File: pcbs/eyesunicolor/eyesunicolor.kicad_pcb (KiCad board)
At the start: 2 copper layers, 21 parts, among them J1 SUPP28, P1 CONN_5X2

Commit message: Dise?o de placa. Acomodamos los leds.
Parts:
- moved D6 387.9 mm to (377.4, 89.4)
- moved D7 378.0 mm to (370.8, 73.2)
- moved D4 369.6 mm to (358.6, 89.4)
- moved D8 368.7 mm to (364.2, 56.9)
- moved D5 368.4 mm to (360.2, 77.2)
- moved D9 360.9 mm to (358.6, 40.1)
- moved D10 357.4 mm to (352.6, 58.4)
- moved D3 351.4 mm to (339.9, 89.4)
- moved D16 350.5 mm to (341.9, 77.2)
- moved D14 346.9 mm to (343.4, 49.3)
- moved D15 343.0 mm to (336.8, 65.0)
- moved D13 333.3 mm to (328.2, 58.4)
- moved D2 333.3 mm to (321.1, 89.4)
- moved D12 327.2 mm to (318.0, 77.2)
- moved D11 320.1 mm to (312.9, 67.6)
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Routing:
- net /BLANK: track 18.0 -> 0.00 mm
- net VCC: track 18.0 -> 0.00 mm

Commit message: Termine la placa. Hay que optimizarla.
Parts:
- R1: value R -> 2.2k
- R2: value R -> 10k
- moved R2 22.9 mm to (321.1, 142.2), turned to 90 degrees
- moved C1 13.3 mm to (335.8, 145.8), turned to 0 degrees
- moved R1 13.2 mm to (316.0, 140.2), turned to 270 degrees
- turned P1 to 180 degrees
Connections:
- D1 pad 2: N-0000020 -> N-0000013
- D10 pad 2: N-0000019 -> N-0000026
- D11 pad 2: N-0000018 -> N-0000029
- D12 pad 2: N-0000017 -> N-0000018
- D13 pad 2: N-0000016 -> N-0000020
- D14 pad 2: N-0000015 -> N-0000017
- D15 pad 2: N-0000014 -> N-0000028
- D16 pad 2: N-0000029 -> N-0000027
- D2 pad 2: N-0000021 -> N-0000019
- D3 pad 2: N-0000022 -> N-0000012
- D6 pad 2: N-0000025 (its old number) -> N-0000016
- D7 pad 2: N-0000026 -> N-0000022
- D8 pad 2: N-0000027 -> N-0000023
- D9 pad 2: N-0000028 -> N-0000021
- J1 pad 1: N-0000020 -> N-0000022
- J1 pad 10: N-0000019 -> N-0000028
- J1 pad 11: N-0000018 -> N-0000020
- J1 pad 12: N-0000017 -> N-0000019
- J1 pad 13: N-0000016 -> N-0000018
- J1 pad 14: N-0000015 -> N-0000029
- J1 pad 15: N-0000029 -> N-0000013
- J1 pad 2: N-0000021 -> N-0000023
- J1 pad 28: N-0000014 -> N-0000016
- J1 pad 3: N-0000022 -> N-0000024
- J1 pad 5: N-0000024 -> N-0000021
- J1 pad 6: N-0000025 (its old number) -> N-0000026
- J1 pad 7: N-0000026 -> N-0000017
- J1 pad 8: N-0000027 -> N-0000012
- J1 pad 9: N-0000028 -> N-0000027
- P1 pad 10: (no net) -> GND
- P1 pad 2: /IREF -> /GSCLK
- P1 pad 4: /GSCLK -> (no net)
- P1 pad 6: VCC -> /IREF
- P1 pad 8: GND -> VCC
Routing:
- net /GSCLK: track 0.00 -> 105.0 mm
- net /IREF: track 0.00 -> 90.5 mm
- net N-0000021: track 0.00 -> 81.5 mm
- net VCC: track 0.00 -> 73.1 mm
- net N-0000017: track 0.00 -> 70.0 mm
- net N-0000023: track 0.00 -> 66.6 mm
- net GND: track 0.00 -> 62.3 mm
- net N-0000026: track 0.00 -> 61.7 mm
- net N-0000020: track 0.00 -> 56.9 mm
- net N-0000028: track 0.00 -> 53.3 mm
- net N-0000029: track 0.00 -> 52.8 mm
- net N-0000022: track 0.00 -> 49.3 mm
- net N-0000016: track 0.00 -> 46.4 mm
- net N-0000024: track 0.00 -> 45.7 mm
- net N-0000018: track 0.00 -> 41.7 mm
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
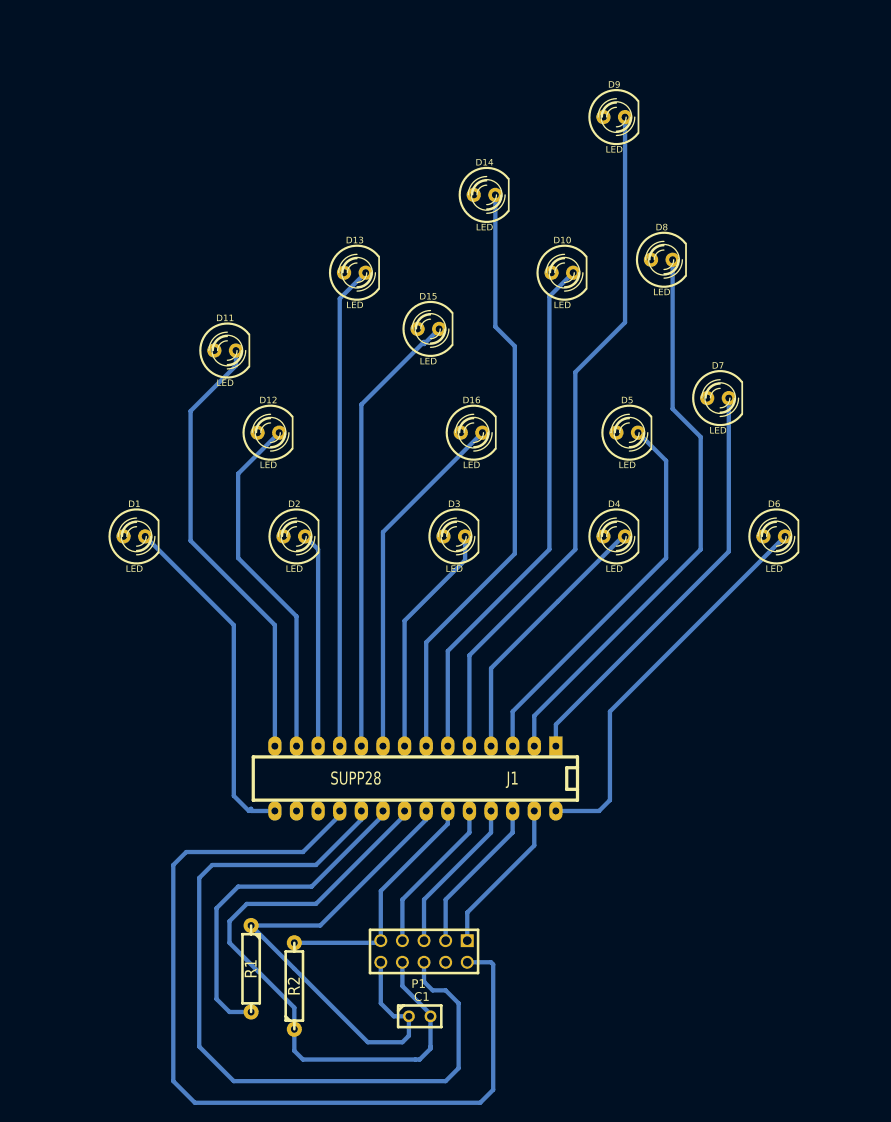
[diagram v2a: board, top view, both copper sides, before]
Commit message: Se termino el PCB del ojo izquierdo, se comenzo a trabajar con el ojo derecho
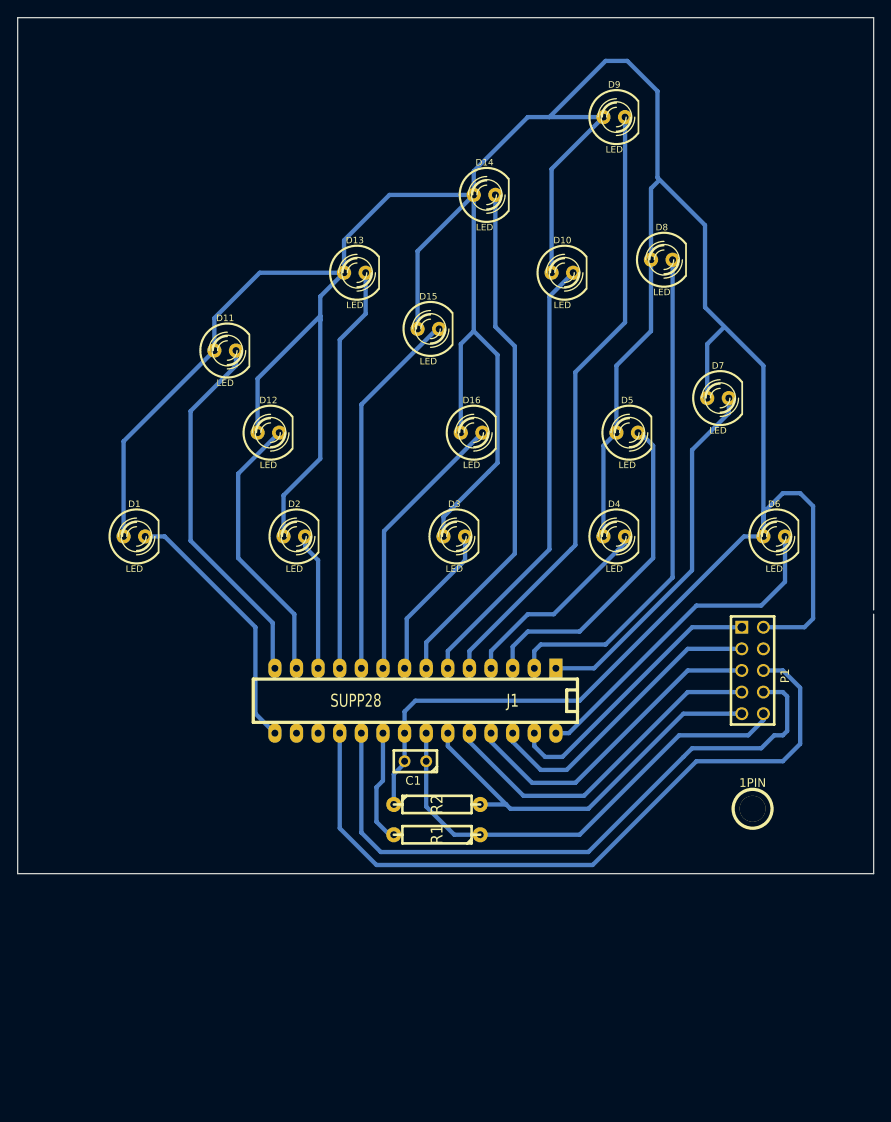
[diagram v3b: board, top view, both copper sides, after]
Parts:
- added 1PIN: P***, 1pin, F.Cu at (374.9, 121.4)
- moved P1 50.8 mm to (374.9, 105.2), turned to 270 degrees
- moved C1 30.0 mm to (335.3, 115.8), turned to 180 degrees
- moved R2 27.1 mm to (337.8, 120.9), turned to 0 degrees
- moved R1 26.9 mm to (337.8, 124.5), turned to 180 degrees
- moved J1 9.14 mm to (335.3, 108.7)
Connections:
- P1 pad 2: /GSCLK -> VCC
- P1 pad 6: /IREF -> /GSCLK
- P1 pad 8: VCC -> /IREF
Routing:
- net VCC: track 73.1 -> 455.8 mm
- net N-0000010: track 40.0 -> 13.4 mm
- net /XLAT: track 18.5 -> 40.7 mm
- net /GSCLK: track 105.0 -> 84.7 mm
- net /SCLK: track 18.5 -> 37.9 mm
- net /BLANK: track 28.8 -> 46.8 mm
- net /SIN: track 18.5 -> 35.9 mm
- net /IREF: track 90.5 -> 75.6 mm
- net /VPRG: track 18.5 -> 32.7 mm
- net N-0000013: track 40.7 -> 30.8 mm
- net N-0000028: track 53.3 -> 43.8 mm
- net N-0000029: track 52.8 -> 43.7 mm
- net N-0000012: track 27.6 -> 18.4 mm
- net N-0000026: track 61.7 -> 52.6 mm
- net N-0000021: track 81.5 -> 72.3 mm
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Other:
- board outline added: 100.6 x 100.6 mm

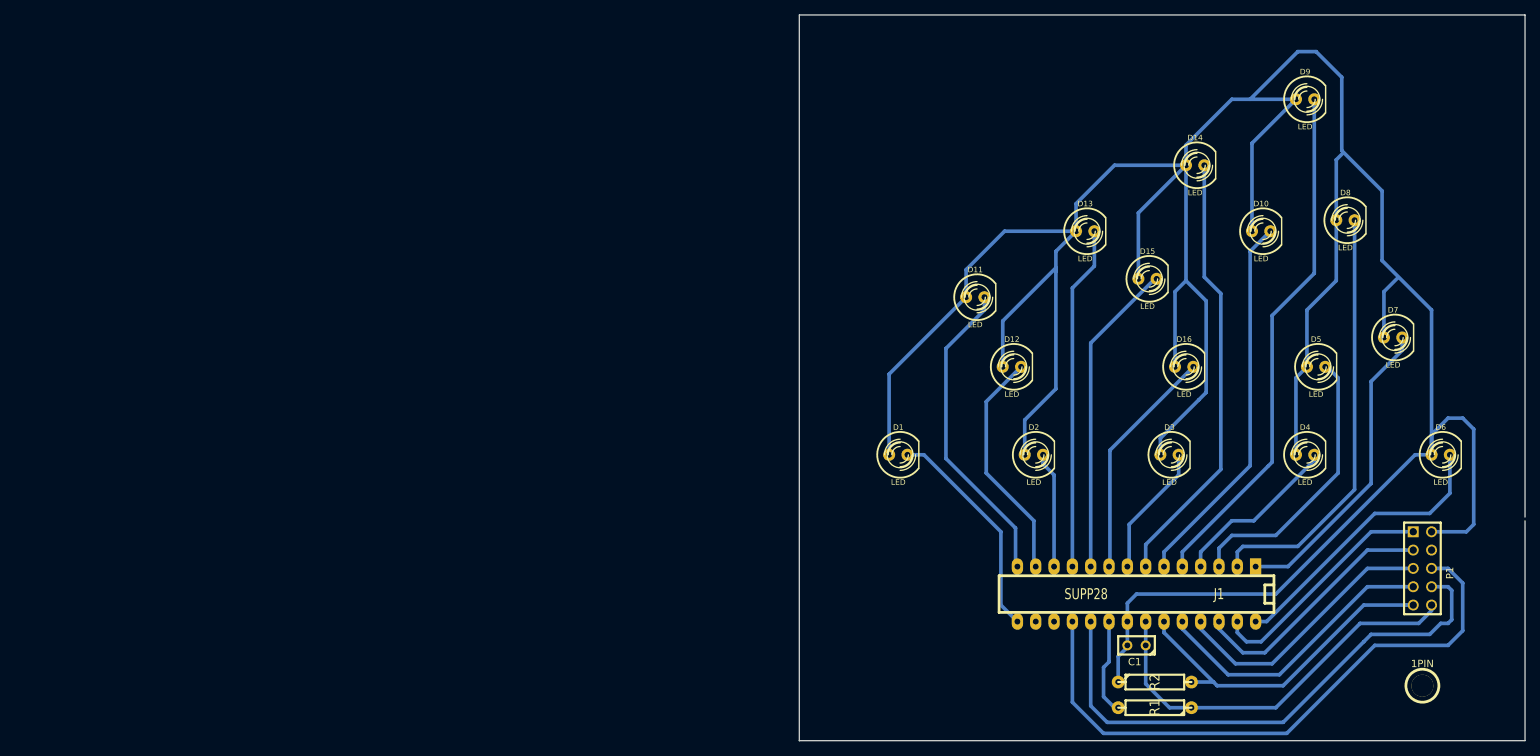
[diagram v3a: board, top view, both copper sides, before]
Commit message: Arme el pcb del ojo derecho. Falta termiar
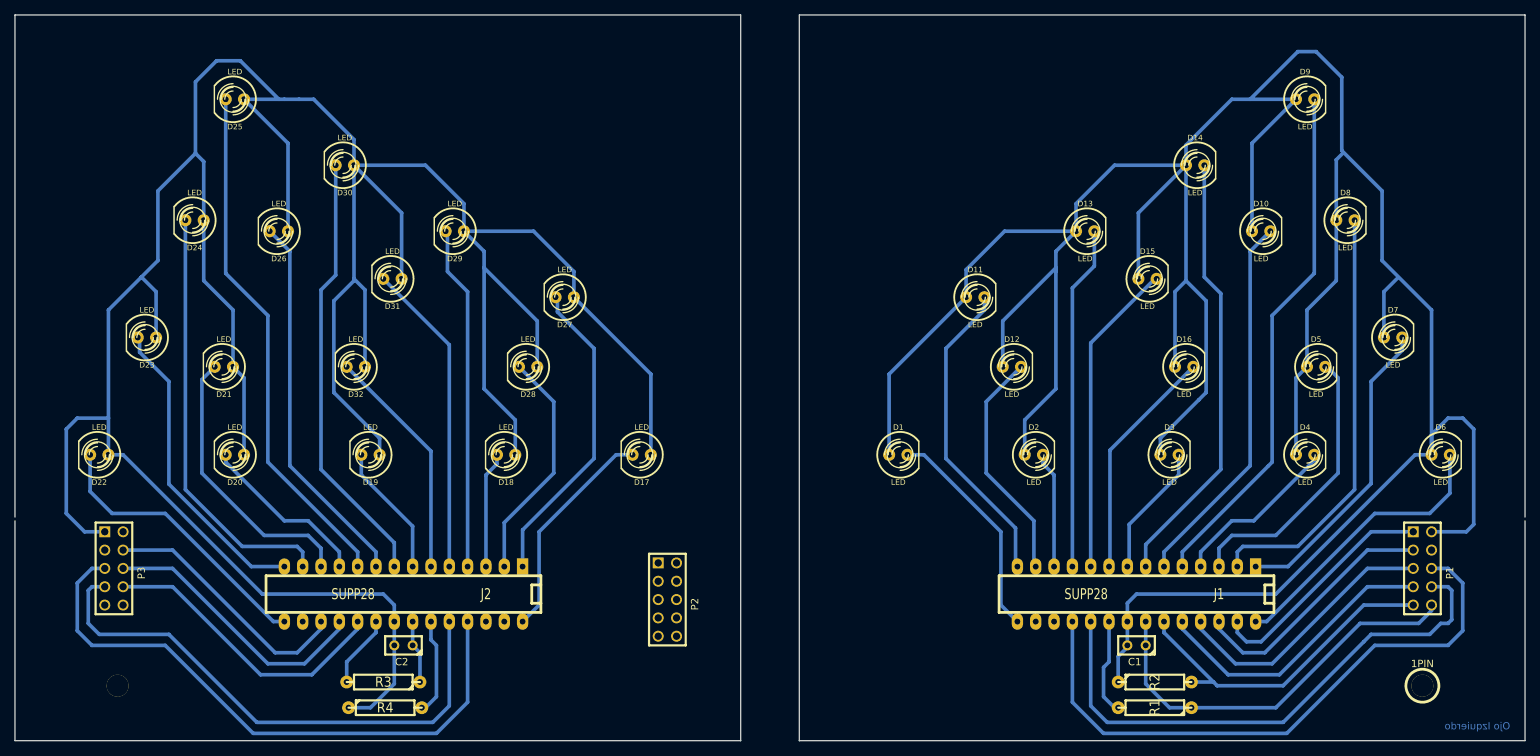
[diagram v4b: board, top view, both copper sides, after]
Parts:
- added 1PIN: P***, 1pin, B.Cu at (194.1, 121.4)
- added C2: C, C1, F.Cu at (233.7, 115.8)
- added D17: LED, LED-5MM, F.Cu at (266.7, 89.4)
- added D18: LED, LED-5MM, F.Cu at (247.9, 89.4)
- added D19: LED, LED-5MM, F.Cu at (229.1, 89.4)
- added D20: LED, LED-5MM, F.Cu at (210.3, 89.4)
- added D21: LED, LED-5MM, F.Cu at (208.8, 77.2)
- added D22: LED, LED-5MM, F.Cu at (191.5, 89.4)
- added D23: LED, LED-5MM, F.Cu at (198.1, 73.2)
- added D24: LED, LED-5MM, F.Cu at (204.7, 56.9)
- added D25: LED, LED-5MM, F.Cu at (210.3, 40.1)
- added D26: LED, LED-5MM, F.Cu at (216.4, 58.4)
- added D27: LED, LED-5MM, F.Cu at (256.0, 67.6)
- added D28: LED, LED-5MM, F.Cu at (251.0, 77.2)
- added D29: LED, LED-5MM, F.Cu at (240.8, 58.4)
- added D30: LED, LED-5MM, F.Cu at (225.6, 49.3)
- added D31: LED, LED-5MM, F.Cu at (232.2, 65.0)
- added D32: LED, LED-5MM, F.Cu at (227.1, 77.2)
- added J2: SUPP28, DIP-28__300_ELL, F.Cu at (233.7, 108.7)
- added P2: CONN_5X2, PIN_ARRAY_5x2, F.Cu at (270.3, 109.5)
- added P3: CONN_5X2, PIN_ARRAY_5x2, F.Cu at (193.5, 105.2)
- added R3: 2.2k, R4-LARGE_PADS, F.Cu at (230.9, 120.9)
- added R4: 10k, R4-LARGE_PADS, F.Cu at (231.1, 124.5)
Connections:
- net /BLANK renamed /BLANK_I
- net /GSCLK renamed /GSCLK_I
- net /IREF renamed /DCPRG_I
- net /SCLK renamed /SCLK_I
- net /SIN renamed /SIN_I
- net /VPRG renamed /VPRG_I
- net /XLAT renamed /XLAT_I
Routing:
- net VCC: track 455.8 -> 909.2 mm
- net /SCLK_D: track 0.00 -> 84.2 mm
- net /XLAT_D: track 0.00 -> 75.4 mm
- net N-0000054: track 0.00 -> 72.3 mm
- net N-0000014: track 0.00 -> 60.7 mm
- net N-0000057: track 0.00 -> 59.2 mm
- net N-0000042: track 0.00 -> 52.6 mm
- net N-0000043: track 0.00 -> 47.7 mm
- net N-0000049: track 0.00 -> 43.7 mm
- net N-0000046: track 0.00 -> 43.7 mm
- net N-0000041: track 0.00 -> 42.8 mm
- net /DCPRG_D: track 0.00 -> 41.2 mm
- net N-0000055: track 0.00 -> 39.5 mm
- net N-0000051: track 0.00 -> 38.8 mm
- net /GSCLK_D: track 0.00 -> 38.5 mm
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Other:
- board size 100.6 x 100.6 mm -> 209.3 x 100.6 mm
- board text added: "Ojo Izquierdo"

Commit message: Intente terminar los ojos, pero no puedo co el ojo derecho. TERMINAR URGENTE
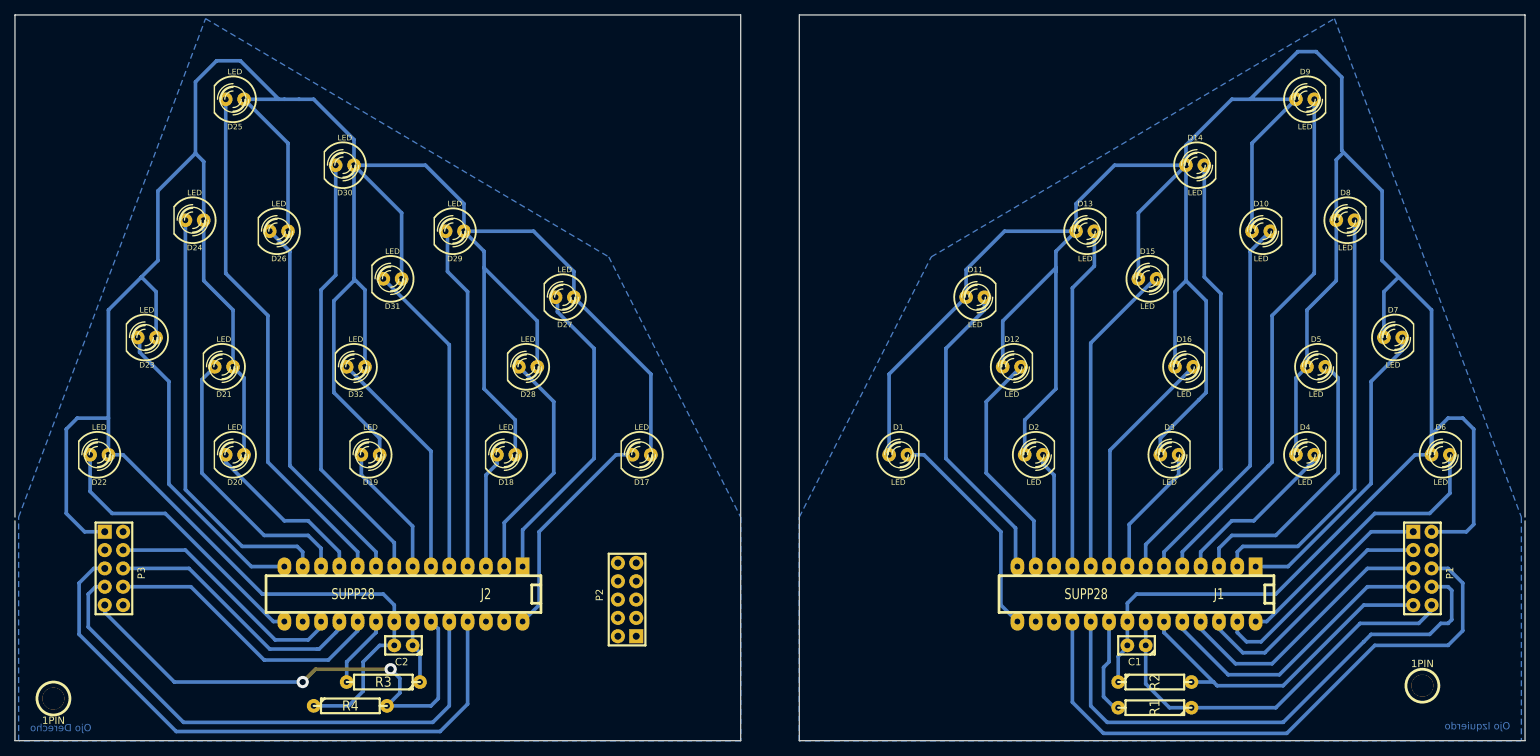
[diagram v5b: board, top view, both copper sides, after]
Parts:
- 1PIN: moved to F.Cu
- moved 1PIN 9.07 mm to (185.2, 123.2)
- moved P2 5.59 mm to (264.7, 109.5), turned to 90 degrees
- moved R4 4.83 mm to (226.3, 124.2)
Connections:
- P2 pad 2: VCC -> /SCLK_D
- P2 pad 5: /SCLK_D -> /GSCLK_D
- P2 pad 6: /GSCLK_D -> /XLAT_D
- P2 pad 7: /XLAT_D -> VCC
- P2 pad 8: /DCPRG_D -> /BLANK_D
- P2 pad 9: /BLANK_D -> /DCPRG_D
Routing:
- net /BLANK_D: track 13.4 -> 70.3 mm, vias 0 -> 2
- net VCC: track 909.2 -> 913.2 mm
- net /GSCLK_D: track 38.5 -> 36.8 mm
- net /SOUT_D: track 36.4 -> 34.8 mm
- net /DCPRG_D: track 41.2 -> 39.7 mm
- added copper zone on B.Cu, net GND
- added copper zone on B.Cu, net VCC
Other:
- board text added: "Ojo Derecho"
